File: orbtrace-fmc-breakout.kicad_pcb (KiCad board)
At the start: 2 copper layers, 78.8 x 69 mm, 34 parts, among them J1 Samtec_ASP-134604-01, J2 Conn_01x02, SW1 SW_SPST, SW2 SW_SPST, SW3 SW_SPST, SW4 SW_SPST, SW5 SW_DIP_x04

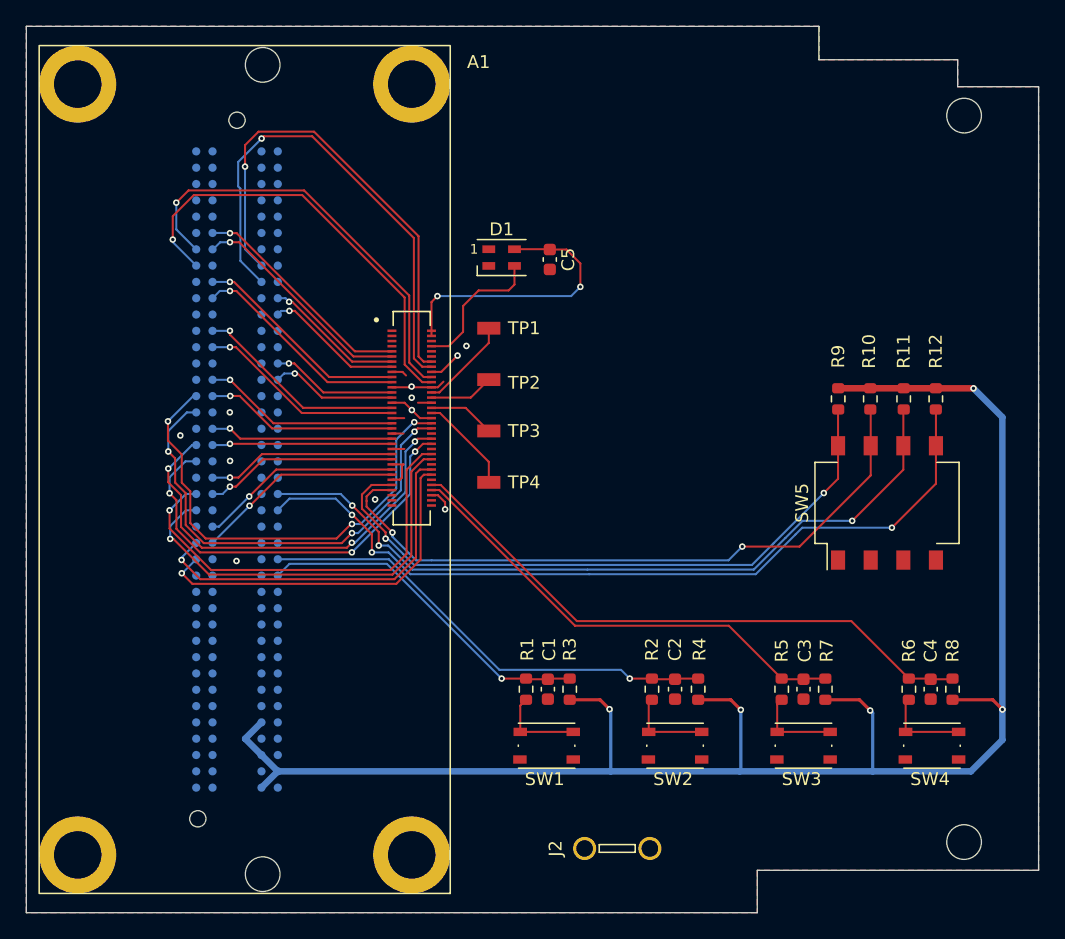
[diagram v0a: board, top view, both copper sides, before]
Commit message: dev: fix for misaligned FMC
This commit fixes the FMC orientation by rotating it 180 degrees.  The
original layout was created while looking at a mirrored view of an
example FMC expansion board - oops.

This update also adds a standard 20-pin 0.1" pitch Arm debug connector
that is wired for SWD only.  In addition there are 2 8-pin 0.1" headers
connected to FPGA IO that can be used for user IO of any sort.
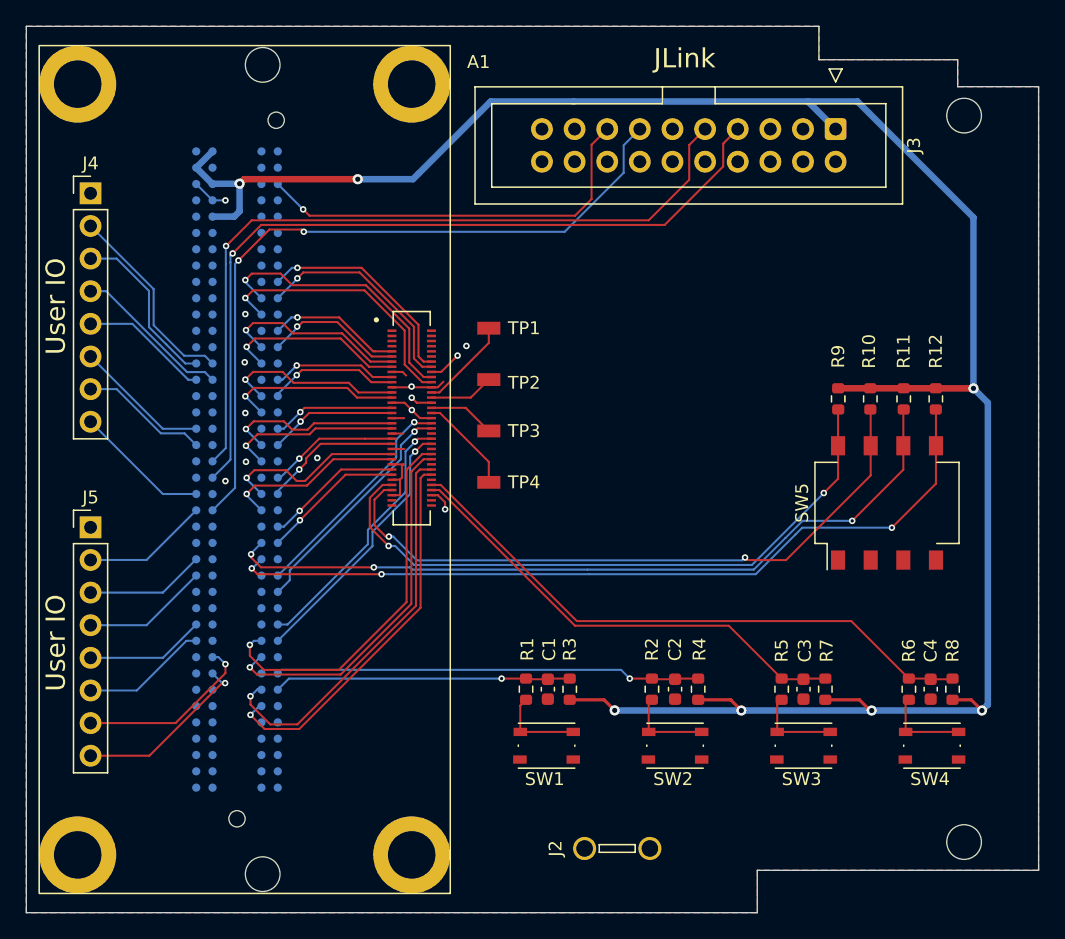
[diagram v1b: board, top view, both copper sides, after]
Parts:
- removed C5: 100nF, Capacitor_SMD:C_0603_1608Metric
- removed D1: SK6805, LED_SMD:LED_SK6805_PLCC4_2.4x2.7mm_P1.3mm
- added J3: Conn_ARM_JTAG_SWD_20, Connector_IDC:IDC-Header_2x10_P2.54mm_Vertical, F.Cu at (153.0, 59.0)
- added J4: Conn_01x08_Male, Connector_PinHeader_2.54mm:PinHeader_1x08_P2.54mm_Vertical, F.Cu at (95.0, 64.0)
- added J5: Conn_01x08_Male, Connector_PinHeader_2.54mm:PinHeader_1x08_P2.54mm_Vertical, F.Cu at (95.0, 90.0)
- turned J1 to 0 degrees
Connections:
- A1 pad 11: /LA00_N_CC -> /LA24_P
- A1 pad 13: /LA06_P -> /LA25_N
- A1 pad 14: /LA01_P_CC -> /LA28_N
- A1 pad 15: /LA06_N -> /LA25_P
- A1 pad 16: /LA01_N_CC -> /LA28_P
- A1 pad 19: /LA03_P -> /LA21_N
- A1 pad 2: +5V -> unconnected-(A1-Pad2)
- A1 pad 20: /LA02_P -> /LA29_N
- A1 pad 21: /LA03_N -> /LA21_P
- A1 pad 22: /LA02_N -> /LA29_P
- A1 pad 25: /LA10_P -> /LA22_N
- A1 pad 27: /LA10_N -> /LA22_P
- A1 pad 31: /LA08_P -> /LA19_N
- A1 pad 33: /LA08_N -> /LA19_P
- A1 pad 37: /LA12_P -> /LA20_N
- A1 pad 38: /LA11_P -> /LA07_N
- A1 pad 39: /LA12_N -> /LA20_P
- A1 pad 4: +5V -> unconnected-(A1-Pad4)
- A1 pad 40: /LA11_N -> /LA07_P
- A1 pad 43: /LA16_P -> /LA15_N
- A1 pad 44: /LA15_P -> /LA04_N
- A1 pad 45: /LA16_N -> /LA15_P
- A1 pad 46: /LA15_N -> /LA04_P
- A1 pad 49: /LA20_P -> /LA16_N
- A1 pad 50: /LA19_P -> /LA03_N
- A1 pad 51: /LA20_N -> /LA16_P
- A1 pad 52: /LA19_N -> /LA03_P
- A1 pad 55: /LA22_P -> /LA11_N
- A1 pad 56: /LA21_P -> /LA00_N_CC
- A1 pad 57: /LA22_N -> /LA11_P
- A1 pad 58: /LA21_N -> /LA00_P_CC
- A1 pad 8: Net-(A1-Pad8) -> unconnected-(A1-Pad8)
- A1 pad 9: /LA00_P_CC -> /LA24_N
- J1 pad C22: /CFG3 -> /LA18_P_CC
- J1 pad C23: /CFG4 -> /LA18_N_CC
- J1 pad C26: /PB3 -> /LA27_P
- J1 pad C27: /PB1 -> /LA27_N
- J1 pad D11: /LA05_P -> unconnected-(J1-PadD11)
- J1 pad D12: /LA05_N -> unconnected-(J1-PadD12)
- J1 pad D14: /LA09_P -> unconnected-(J1-PadD14)
- J1 pad D15: /LA09_N -> unconnected-(J1-PadD15)
- J1 pad D17: /LA13_P -> unconnected-(J1-PadD17)
- J1 pad D18: /LA13_N -> /SWO
- J1 pad D20: /LA17_P_CC -> /SWDIO
- J1 pad D21: /LA17_N_CC -> /SWDCLK
- J1 pad D23: /LA23_P -> unconnected-(J1-PadD23)
- J1 pad D24: /LA23_N -> unconnected-(J1-PadD24)
- J1 pad G12: /LA08_P -> unconnected-(J1-PadG12)
- J1 pad G13: /LA08_N -> unconnected-(J1-PadG13)
- J1 pad G15: /LA12_P -> /CFG4
- J1 pad G16: /LA12_N -> /CFG3
- J1 pad G33: /LA31_P -> unconnected-(J1-PadG33)
- J1 pad G34: /LA31_N -> unconnected-(J1-PadG34)
- J1 pad G36: /LA33_P -> unconnected-(J1-PadG36)
- J1 pad G37: /LA33_N -> unconnected-(J1-PadG37)
- J1 pad H34: /LA30_P -> unconnected-(J1-PadH34)
- J1 pad H35: /LA30_N -> unconnected-(J1-PadH35)
- J1 pad H37: /LA32_P -> unconnected-(J1-PadH37)
- J1 pad H38: /LA32_N -> /nRESET
- J1 pad H7: /LA02_P -> /PB1
- J1 pad H8: /LA02_N -> /PB3
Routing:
- net /SWDIO: track 0.00 -> 62.5 mm, vias 0 -> 1
- net /SWDCLK: track 0.00 -> 59.8 mm, vias 0 -> 1
- net /SWO: track 0.00 -> 57.2 mm, vias 0 -> 2
- net +3V3: track 133.0 -> 169.0 mm, vias 5 -> 7
- net /LA02_N: track 34.5 -> 0.00 mm, vias 1 -> 0
- net /LA02_P: track 33.6 -> 0.00 mm, vias 1 -> 0
- net /nRESET: track 0.00 -> 31.9 mm, vias 0 -> 1
- net /LA11_P: track 36.9 -> 11.1 mm, vias 3 -> 1
- net /LA11_N: track 36.1 -> 10.7 mm, vias 3 -> 1
- net /LA01_N_CC: track 38.9 -> 14.0 mm
- net /LA01_P_CC: track 37.8 -> 14.1 mm
- net /LA19_P: track 33.3 -> 9.95 mm
- net /LA19_N: track 32.6 -> 9.56 mm
- net /LA15_P: track 33.5 -> 10.8 mm, vias 3 -> 1
- net /LA15_N: track 32.7 -> 10.1 mm, vias 3 -> 1
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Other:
- board text added: "IDEX Biometrics Ltd Revision 0.2 2023/08/04 Mini-ITX FMC Orbtrace Breakout Board"
- board text added: "JLink"
- board text added: "User IO"
